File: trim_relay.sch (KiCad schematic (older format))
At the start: 27 parts, among them J1 Conn_01x01, J10 Conn_01x01, J11 Conn_01x01, J12 Conn_01x01, J2 Conn_01x01, J3 Conn_01x01, J4 Conn_01x01, J5 Conn_01x01, J6 Conn_01x01, J7 Conn_01x01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

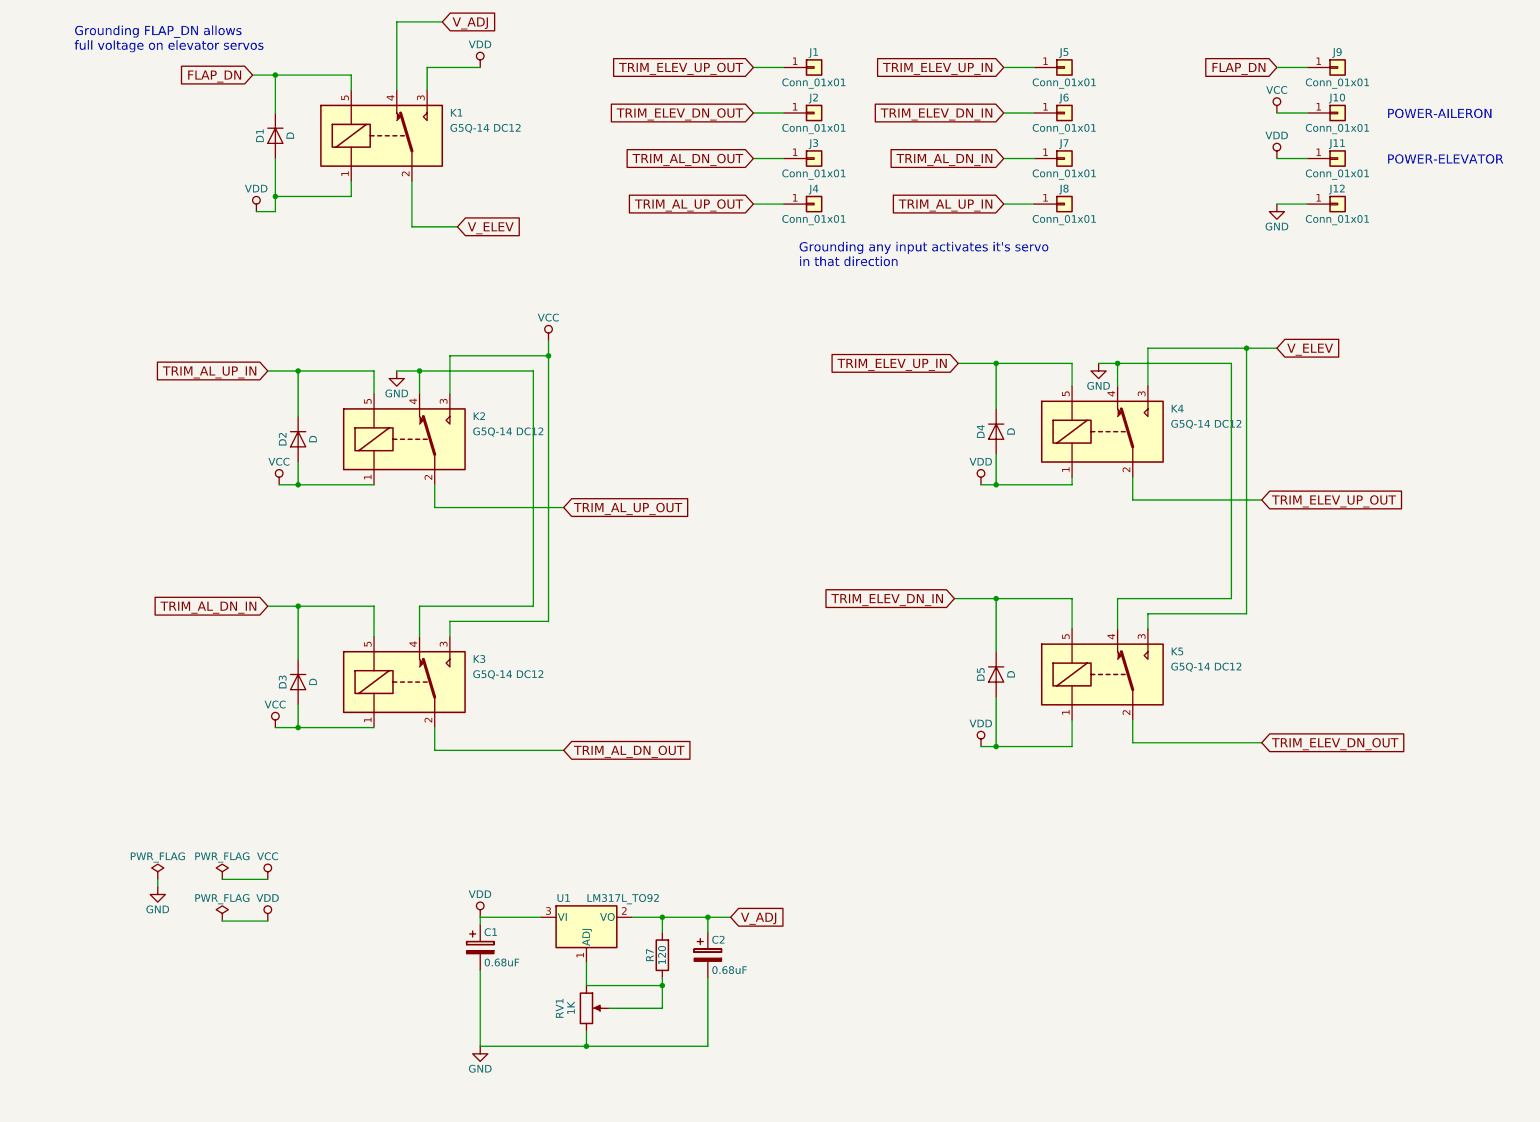
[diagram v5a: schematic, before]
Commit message: Added solder bridges, redid routing
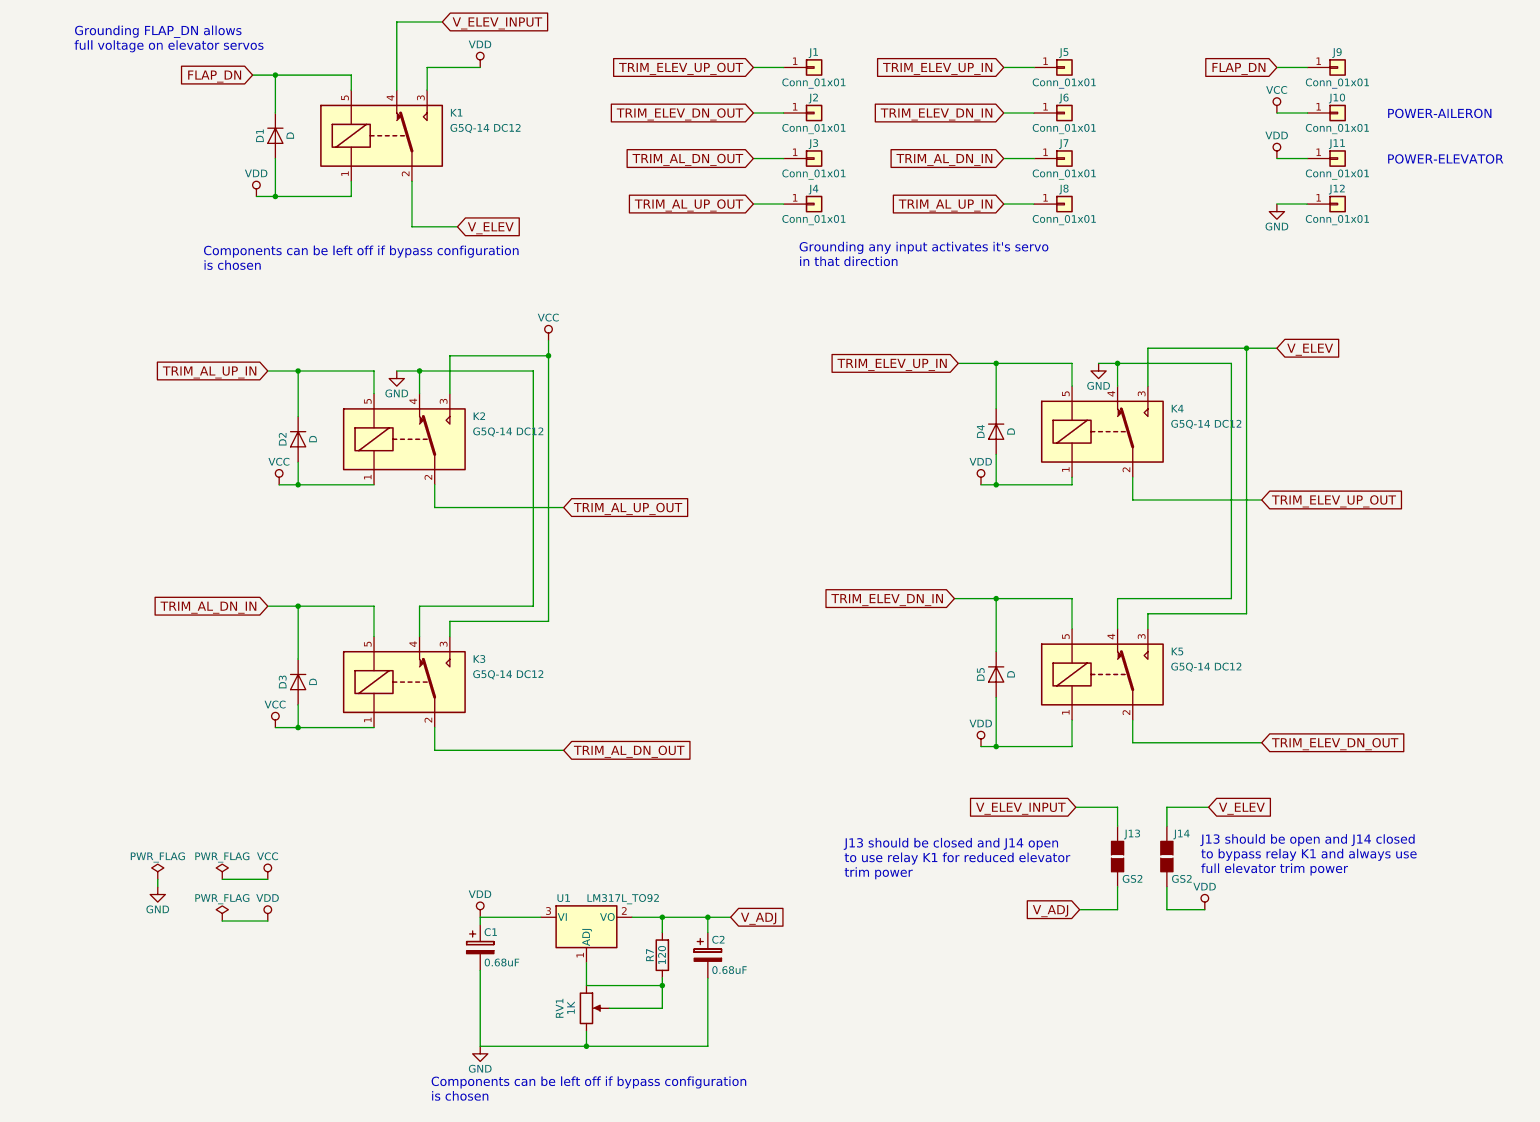
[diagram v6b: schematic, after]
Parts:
- added J13, J14: GS2, Connectors:GS2, symbol GS2
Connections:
- net VDD: now also J14.2 (G2)
- net V_ADJ: now also J13.2 (G2); no longer K1.4
- net V_ELEV: now also J14.1 (G1)
- new net V_ELEV_INPUT: J13.1 (G1), K1.4
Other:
- note added: "Components can be left off if bypass configuration\nis chosen"
- note added: "J13 should be closed and J14 open \nto use relay K1 for reduced elevator \ntrim power"
- note added: "J13 should be open and J14 closed \nto bypass relay K1 and always use \nfull elevator trim power"
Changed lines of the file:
@@
 $EndComp
-Wire Wire Line
-	2050 1550 2050 1900
 Wire Wire Line
 	2050 1250 2050 1000
@@
 TRIM_ELEV_DN_IN
 Wire Wire Line
-	8350 4450 8350 2900
+	8350 2900 8350 4450
 Wire Wire Line
 	7600 4450 7600 4650
@@
 	7700 5400 7700 5250
 $Comp
-L GND #PWR01
+L GND #PWR14
 U 1 1 5B5AE318
 P 7475 2900
-F 0 "#PWR01" H 7475 2650 50  0001 C CNN
+F 0 "#PWR14" H 7475 2650 50  0001 C CNN
 F 1 "GND" H 7475 2750 50  0000 C CNN
 F 2 "" H 7475 2900 50  0001 C CNN
@@
 Connection ~ 4100 7400
 $Comp
-L GND #PWR02
+L GND #PWR10
 U 1 1 5B5AF061
 P 3400 7400
-F 0 "#PWR02" H 3400 7150 50  0001 C CNN
+F 0 "#PWR10" H 3400 7150 50  0001 C CNN
 F 1 "GND" H 3400 7250 50  0000 C CNN
 F 2 "" H 3400 7400 50  0001 C CNN
@@
 	5200 1850 5400 1850
 Text GLabel 3150 650  2    60   Input ~ 0
-V_ADJ
+V_ELEV_INPUT
 Wire Wire Line
 	2850 650  3150 650
@@
 	8650 1850 8850 1850
 $Comp
-L GND #PWR03
+L GND #PWR18
 U 1 1 5B5FD5D6
 P 8650 1850
-F 0 "#PWR03" H 8650 1600 50  0001 C CNN
+F 0 "#PWR18" H 8650 1600 50  0001 C CNN
 F 1 "GND" H 8650 1700 50  0000 C CNN
 F 2 "" H 8650 1850 50  0001 C CNN
@@
 $EndComp
 Wire Wire Line
-	2050 1800 2550 1800
+	1925 1800 2550 1800
 Connection ~ 2050 1800
 Wire Wire Line
@@
 $EndComp
 $Comp
-L VCC #PWR04
+L VCC #PWR16
 U 1 1 5B65F2C6
 P 8650 1250
-F 0 "#PWR04" H 8650 1100 50  0001 C CNN
+F 0 "#PWR16" H 8650 1100 50  0001 C CNN
 F 1 "VCC" H 8650 1400 50  0000 C CNN
 F 2 "" H 8650 1250 50  0001 C CNN
@@
 $EndComp
 $Comp
-L VDD #PWR05
+L VDD #PWR17
 U 1 1 5B65F32E
 P 8650 1550
-F 0 "#PWR05" H 8650 1400 50  0001 C CNN
+F 0 "#PWR17" H 8650 1400 50  0001 C CNN
 F 1 "VDD" H 8650 1700 50  0000 C CNN
 F 2 "" H 8650 1550 50  0001 C CNN
@@
 POWER-AILERON
 $Comp
-L VDD #PWR06
+L VDD #PWR13
 U 1 1 5B6627AC
 P 6700 5425
-F 0 "#PWR06" H 6700 5275 50  0001 C CNN
+F 0 "#PWR13" H 6700 5275 50  0001 C CNN
 F 1 "VDD" H 6700 5575 50  0000 C CNN
 F 2 "" H 6700 5425 50  0001 C CNN
@@
 $EndComp
 $Comp
-L VDD #PWR07
+L VDD #PWR9
 U 1 1 5B6633BC
 P 3400 6550
-F 0 "#PWR07" H 3400 6400 50  0001 C CNN
+F 0 "#PWR9" H 3400 6400 50  0001 C CNN
 F 1 "VDD" H 3400 6700 50  0000 C CNN
 F 2 "" H 3400 6550 50  0001 C CNN
@@
 $EndComp
 $Comp
-L VCC #PWR08
+L VCC #PWR11
 U 1 1 5B663EC5
 P 3850 2750
-F 0 "#PWR08" H 3850 2600 50  0001 C CNN
+F 0 "#PWR11" H 3850 2600 50  0001 C CNN
 F 1 "VCC" H 3850 2900 50  0000 C CNN
 F 2 "" H 3850 2750 50  0001 C CNN
@@
 $EndComp
 $Comp
-L VCC #PWR09
+L VCC #PWR6
 U 1 1 5B664FE0
 P 2075 3700
-F 0 "#PWR09" H 2075 3550 50  0001 C CNN
+F 0 "#PWR6" H 2075 3550 50  0001 C CNN
 F 1 "VCC" H 2075 3850 50  0000 C CNN
 F 2 "" H 2075 3700 50  0001 C CNN
@@
 $EndComp
 $Comp
-L VDD #PWR010
+L VDD #PWR8
 U 1 1 5B665897
 P 3400 950
-F 0 "#PWR010" H 3400 800 50  0001 C CNN
+F 0 "#PWR8" H 3400 800 50  0001 C CNN
 F 1 "VDD" H 3400 1100 50  0000 C CNN
 F 2 "" H 3400 950 50  0001 C CNN
@@
 $EndComp
 $Comp
-L VDD #PWR011
+L VDD #PWR2
 U 1 1 5B66599E
-P 1925 1900
-F 0 "#PWR011" H 1925 1750 50  0001 C CNN
-F 1 "VDD" H 1925 2050 50  0000 C CNN
-F 2 "" H 1925 1900 50  0001 C CNN
-F 3 "" H 1925 1900 50  0001 C CNN
-	1    1925 1900
-	1    0    0    -1
-$EndComp
-Wire Wire Line
-	2050 1900 1925 1900
+P 1925 1800
+F 0 "#PWR2" H 1925 1650 50  0001 C CNN
+F 1 "VDD" H 1925 1950 50  0000 C CNN
+F 2 "" H 1925 1800 50  0001 C CNN
+F 3 "" H 1925 1800 50  0001 C CNN
+	1    1925 1800
+	1    0    0    -1
+$EndComp
 Wire Wire Line
 	2200 3250 2200 2950
@@
 	2000 4500 2700 4500
 $Comp
-L GND #PWR012
+L GND #PWR7
 U 1 1 5B6D2F47
 P 2850 2950
-F 0 "#PWR012" H 2850 2700 50  0001 C CNN
+F 0 "#PWR7" H 2850 2700 50  0001 C CNN
 F 1 "GND" H 2850 2800 50  0000 C CNN
 F 2 "" H 2850 2950 50  0001 C CNN
@@
 	3750 4500 3000 4500
 $Comp
-L VCC #PWR013
+L VCC #PWR5
 U 1 1 5B6D432D
 P 2050 5300
-F 0 "#PWR013" H 2050 5150 50  0001 C CNN
+F 0 "#PWR5" H 2050 5150 50  0001 C CNN
 F 1 "VCC" H 2050 5450 50  0000 C CNN
 F 2 "" H 2050 5300 50  0001 C CNN
@@
 $EndComp
 Wire Wire Line
-	8350 2900 7475 2900
-Wire Wire Line
-	7300 2900 6550 2900
-Wire Wire Line
-	7300 4450 6525 4450
+	7475 2900 8350 2900
+Wire Wire Line
+	6550 2900 7300 2900
+Wire Wire Line
+	6525 4450 7300 4450
 Wire Wire Line
 	6800 5425 6800 5100
 Wire Wire Line
-	7600 4450 8350 4450
+	8350 4450 7600 4450
 Wire Wire Line
 	6700 5425 7300 5425
 $Comp
-L VDD #PWR014
+L VDD #PWR12
 U 1 1 5B6D6DBC
 P 6700 3700
-F 0 "#PWR014" H 6700 3550 50  0001 C CNN
+F 0 "#PWR12" H 6700 3550 50  0001 C CNN
 F 1 "VDD" H 6700 3850 50  0000 C CNN
 F 2 "" H 6700 3700 50  0001 C CNN
@@
 	6800 3700 6800 3500
 $Comp
-L PWR_FLAG #FLG015
+L PWR_FLAG #FLG1
 U 1 1 5B6DC21E
 P 1275 6300
-F 0 "#FLG015" H 1275 6375 50  0001 C CNN
+F 0 "#FLG1" H 1275 6375 50  0001 C CNN
 F 1 "PWR_FLAG" H 1275 6450 50  0000 C CNN
 F 2 "" H 1275 6300 50  0001 C CNN
@@
 $EndComp
 $Comp
-L GND #PWR016
+L GND #PWR1
 U 1 1 5B6DC2D2
 P 1275 6350
-F 0 "#PWR016" H 1275 6100 50  0001 C CNN
+F 0 "#PWR1" H 1275 6100 50  0001 C CNN
 F 1 "GND" H 1275 6200 50  0000 C CNN
 F 2 "" H 1275 6350 50  0001 C CNN
@@
 	1275 6300 1275 6350
 $Comp
-L PWR_FLAG #FLG017
+L PWR_FLAG #FLG2
 U 1 1 5B6DC406
 P 1700 6300
-F 0 "#FLG017" H 1700 6375 50  0001 C CNN
+F 0 "#FLG2" H 1700 6375 50  0001 C CNN
 F 1 "PWR_FLAG" H 1700 6450 50  0000 C CNN
 F 2 "" H 1700 6300 50  0001 C CNN
@@
 $EndComp
 $Comp
-L VCC #PWR018
+L VCC #PWR3
 U 1 1 5B6DC78C
 P 2000 6300
-F 0 "#PWR018" H 2000 6150 50  0001 C CNN
+F 0 "#PWR3" H 2000 6150 50  0001 C CNN
 F 1 "VCC" H 2000 6450 50  0000 C CNN
 F 2 "" H 2000 6300 50  0001 C CNN
@@
 $EndComp
 $Comp
-L VDD #PWR019
+L VDD #PWR4
 U 1 1 5B6DC7E8
 P 2000 6575
-F 0 "#PWR019" H 2000 6425 50  0001 C CNN
+F 0 "#PWR4" H 2000 6425 50  0001 C CNN
 F 1 "VDD" H 2000 6725 50  0000 C CNN
 F 2 "" H 2000 6575 50  0001 C CNN
@@
 	1700 6300 2000 6300
 $Comp
-L PWR_FLAG #FLG020
+L PWR_FLAG #FLG3
 U 1 1 5B6DCB1E
 P 1700 6575
-F 0 "#FLG020" H 1700 6650 50  0001 C CNN
+F 0 "#FLG3" H 1700 6650 50  0001 C CNN
 F 1 "PWR_FLAG" H 1700 6725 50  0000 C CNN
 F 2 "" H 1700 6575 50  0001 C CNN
@@
 Wire Wire Line
 	1700 6575 2000 6575
+Wire Wire Line
+	2050 1550 2050 1800
+Text GLabel 7350 6500 0    60   Input ~ 0
+V_ADJ
+$Comp
+L VDD #PWR15
+U 1 1 5B6F2A6F
+P 8175 6500
+F 0 "#PWR15" H 8175 6350 50  0001 C CNN
+F 1 "VDD" H 8175 6650 50  0000 C CNN
+F 2 "" H 8175 6500 50  0001 C CNN
+F 3 "" H 8175 6500 50  0001 C CNN
+	1    8175 6500
+	1    0    0    -1
+$EndComp
+Text GLabel 7325 5825 0    60   Input ~ 0
+V_ELEV_INPUT
+$Comp
+L GS2 J13
+U 1 1 5B756803
+P 7600 6150
+F 0 "J13" H 7700 6300 50  0000 C CNN
+F 1 "GS2" H 7700 6001 50  0000 C CNN
+F 2 "Connectors:GS2" V 7674 6150 50  0001 C CNN
+F 3 "" H 7600 6150 50  0001 C CNN
+	1    7600 6150
+	1    0    0    -1
+$EndComp
+$Comp
+L GS2 J14
+U 1 1 5B756A07
+P 7925 6150
+F 0 "J14" H 8025 6300 50  0000 C CNN
+F 1 "GS2" H 8025 6001 50  0000 C CNN
+F 2 "Connectors:GS2" V 7999 6150 50  0001 C CNN
+F 3 "" H 7925 6150 50  0001 C CNN
+	1    7925 6150
+	1    0    0    -1
+$EndComp
+Wire Wire Line
+	7600 5950 7600 5825
+Wire Wire Line
+	7925 5825 7925 5950
+Wire Wire Line
+	7600 6350 7600 6500
+Wire Wire Line
+	7925 6350 7925 6500
+Wire Wire Line
+	7925 6500 8175 6500
+Wire Wire Line
+	7600 6500 7350 6500
+Text GLabel 8200 5825 2    60   Input ~ 0
+V_ELEV
+Wire Wire Line
+	7925 5825 8200 5825
+Wire Wire Line
+	7600 5825 7325 5825
+Text Notes 5800 6300 0    60   ~ 0
+J13 should be closed and J14 open \nto use relay K1 for reduced elevator \ntrim power
+Text Notes 8150 6275 0    60   ~ 0
+J13 should be open and J14 closed \nto bypass relay K1 and always use \nfull elevator trim power
+Text Notes 3075 7775 0    60   ~ 0
+Components can be left off if bypass configuration\nis chosen
+Text Notes 1575 2300 0    60   ~ 0
+Components can be left off if bypass configuration\nis chosen
 $EndSCHEMATC

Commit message: Final version
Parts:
- U1: footprint TO_SOT_Packages_THT:TO-92_Horizontal2_Inline_Narrow_Oval -> TO_SOT_Packages_THT:TO-220-3_Horizontal
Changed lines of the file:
@@
 	7700 5400 7700 5250
 $Comp
-L GND #PWR14
+L GND #PWR01
 U 1 1 5B5AE318
 P 7475 2900
-F 0 "#PWR14" H 7475 2650 50  0001 C CNN
+F 0 "#PWR01" H 7475 2650 50  0001 C CNN
 F 1 "GND" H 7475 2750 50  0000 C CNN
 F 2 "" H 7475 2900 50  0001 C CNN
@@
 F 0 "U1" H 3950 6675 50  0000 C CNN
 F 1 "LM317L_TO92" H 4100 6675 50  0000 L CNN
-F 2 "TO_SOT_Packages_THT:TO-92_Horizontal2_Inline_Narrow_Oval" H 4100 6775 50  0001 C CIN
+F 2 "TO_SOT_Packages_THT:TO-220-3_Horizontal" H 4100 6775 50  0001 C CIN
 F 3 "" H 4100 6550 50  0001 C CNN
 	1    4100 6550
@@
 Connection ~ 4100 7400
 $Comp
-L GND #PWR10
+L GND #PWR02
 U 1 1 5B5AF061
 P 3400 7400
-F 0 "#PWR10" H 3400 7150 50  0001 C CNN
+F 0 "#PWR02" H 3400 7150 50  0001 C CNN
 F 1 "GND" H 3400 7250 50  0000 C CNN
 F 2 "" H 3400 7400 50  0001 C CNN
@@
 	8650 1850 8850 1850
 $Comp
-L GND #PWR18
+L GND #PWR03
 U 1 1 5B5FD5D6
 P 8650 1850
-F 0 "#PWR18" H 8650 1600 50  0001 C CNN
+F 0 "#PWR03" H 8650 1600 50  0001 C CNN
 F 1 "GND" H 8650 1700 50  0000 C CNN
 F 2 "" H 8650 1850 50  0001 C CNN
@@
 $EndComp
 $Comp
-L VCC #PWR16
+L VCC #PWR04
 U 1 1 5B65F2C6
 P 8650 1250
-F 0 "#PWR16" H 8650 1100 50  0001 C CNN
+F 0 "#PWR04" H 8650 1100 50  0001 C CNN
 F 1 "VCC" H 8650 1400 50  0000 C CNN
 F 2 "" H 8650 1250 50  0001 C CNN
@@
 $EndComp
 $Comp
-L VDD #PWR17
+L VDD #PWR05
 U 1 1 5B65F32E
 P 8650 1550
-F 0 "#PWR17" H 8650 1400 50  0001 C CNN
+F 0 "#PWR05" H 8650 1400 50  0001 C CNN
 F 1 "VDD" H 8650 1700 50  0000 C CNN
 F 2 "" H 8650 1550 50  0001 C CNN
@@
 POWER-AILERON
 $Comp
-L VDD #PWR13
+L VDD #PWR06
 U 1 1 5B6627AC
 P 6700 5425
-F 0 "#PWR13" H 6700 5275 50  0001 C CNN
+F 0 "#PWR06" H 6700 5275 50  0001 C CNN
 F 1 "VDD" H 6700 5575 50  0000 C CNN
 F 2 "" H 6700 5425 50  0001 C CNN
@@
 $EndComp
 $Comp
-L VDD #PWR9
+L VDD #PWR07
 U 1 1 5B6633BC
 P 3400 6550
-F 0 "#PWR9" H 3400 6400 50  0001 C CNN
+F 0 "#PWR07" H 3400 6400 50  0001 C CNN
 F 1 "VDD" H 3400 6700 50  0000 C CNN
 F 2 "" H 3400 6550 50  0001 C CNN
@@
 $EndComp
 $Comp
-L VCC #PWR11
+L VCC #PWR08
 U 1 1 5B663EC5
 P 3850 2750
-F 0 "#PWR11" H 3850 2600 50  0001 C CNN
+F 0 "#PWR08" H 3850 2600 50  0001 C CNN
 F 1 "VCC" H 3850 2900 50  0000 C CNN
 F 2 "" H 3850 2750 50  0001 C CNN
@@
 $EndComp
 $Comp
-L VCC #PWR6
+L VCC #PWR09
 U 1 1 5B664FE0
 P 2075 3700
-F 0 "#PWR6" H 2075 3550 50  0001 C CNN
+F 0 "#PWR09" H 2075 3550 50  0001 C CNN
 F 1 "VCC" H 2075 3850 50  0000 C CNN
 F 2 "" H 2075 3700 50  0001 C CNN
@@
 $EndComp
 $Comp
-L VDD #PWR8
+L VDD #PWR010
 U 1 1 5B665897
 P 3400 950
-F 0 "#PWR8" H 3400 800 50  0001 C CNN
+F 0 "#PWR010" H 3400 800 50  0001 C CNN
 F 1 "VDD" H 3400 1100 50  0000 C CNN
 F 2 "" H 3400 950 50  0001 C CNN
@@
 $EndComp
 $Comp
-L VDD #PWR2
+L VDD #PWR011
 U 1 1 5B66599E
 P 1925 1800
-F 0 "#PWR2" H 1925 1650 50  0001 C CNN
+F 0 "#PWR011" H 1925 1650 50  0001 C CNN
 F 1 "VDD" H 1925 1950 50  0000 C CNN
 F 2 "" H 1925 1800 50  0001 C CNN
@@
 	2000 4500 2700 4500
 $Comp
-L GND #PWR7
+L GND #PWR012
 U 1 1 5B6D2F47
 P 2850 2950
-F 0 "#PWR7" H 2850 2700 50  0001 C CNN
+F 0 "#PWR012" H 2850 2700 50  0001 C CNN
 F 1 "GND" H 2850 2800 50  0000 C CNN
 F 2 "" H 2850 2950 50  0001 C CNN
@@
 	3750 4500 3000 4500
 $Comp
-L VCC #PWR5
+L VCC #PWR013
 U 1 1 5B6D432D
 P 2050 5300
-F 0 "#PWR5" H 2050 5150 50  0001 C CNN
+F 0 "#PWR013" H 2050 5150 50  0001 C CNN
 F 1 "VCC" H 2050 5450 50  0000 C CNN
 F 2 "" H 2050 5300 50  0001 C CNN
@@
 	6700 5425 7300 5425
 $Comp
-L VDD #PWR12
+L VDD #PWR014
 U 1 1 5B6D6DBC
 P 6700 3700
-F 0 "#PWR12" H 6700 3550 50  0001 C CNN
+F 0 "#PWR014" H 6700 3550 50  0001 C CNN
 F 1 "VDD" H 6700 3850 50  0000 C CNN
 F 2 "" H 6700 3700 50  0001 C CNN
@@
 	6800 3700 6800 3500
 $Comp
-L PWR_FLAG #FLG1
+L PWR_FLAG #FLG015
 U 1 1 5B6DC21E
 P 1275 6300
-F 0 "#FLG1" H 1275 6375 50  0001 C CNN
+F 0 "#FLG015" H 1275 6375 50  0001 C CNN
 F 1 "PWR_FLAG" H 1275 6450 50  0000 C CNN
 F 2 "" H 1275 6300 50  0001 C CNN
@@
 $EndComp
 $Comp
-L GND #PWR1
+L GND #PWR016
 U 1 1 5B6DC2D2
 P 1275 6350
-F 0 "#PWR1" H 1275 6100 50  0001 C CNN
+F 0 "#PWR016" H 1275 6100 50  0001 C CNN
 F 1 "GND" H 1275 6200 50  0000 C CNN
 F 2 "" H 1275 6350 50  0001 C CNN
@@
 	1275 6300 1275 6350
 $Comp
-L PWR_FLAG #FLG2
+L PWR_FLAG #FLG017
 U 1 1 5B6DC406
 P 1700 6300
-F 0 "#FLG2" H 1700 6375 50  0001 C CNN
+F 0 "#FLG017" H 1700 6375 50  0001 C CNN
 F 1 "PWR_FLAG" H 1700 6450 50  0000 C CNN
 F 2 "" H 1700 6300 50  0001 C CNN
@@
 $EndComp
 $Comp
-L VCC #PWR3
+L VCC #PWR018
 U 1 1 5B6DC78C
 P 2000 6300
-F 0 "#PWR3" H 2000 6150 50  0001 C CNN
+F 0 "#PWR018" H 2000 6150 50  0001 C CNN
 F 1 "VCC" H 2000 6450 50  0000 C CNN
 F 2 "" H 2000 6300 50  0001 C CNN
@@
 $EndComp
 $Comp
-L VDD #PWR4
+L VDD #PWR019
 U 1 1 5B6DC7E8
 P 2000 6575
-F 0 "#PWR4" H 2000 6425 50  0001 C CNN
+F 0 "#PWR019" H 2000 6425 50  0001 C CNN
 F 1 "VDD" H 2000 6725 50  0000 C CNN
 F 2 "" H 2000 6575 50  0001 C CNN
@@
 	1700 6300 2000 6300
 $Comp
-L PWR_FLAG #FLG3
+L PWR_FLAG #FLG020
 U 1 1 5B6DCB1E
 P 1700 6575
-F 0 "#FLG3" H 1700 6650 50  0001 C CNN
+F 0 "#FLG020" H 1700 6650 50  0001 C CNN
 F 1 "PWR_FLAG" H 1700 6725 50  0000 C CNN
 F 2 "" H 1700 6575 50  0001 C CNN
@@
 V_ADJ
 $Comp
-L VDD #PWR15
+L VDD #PWR021
 U 1 1 5B6F2A6F
 P 8175 6500
-F 0 "#PWR15" H 8175 6350 50  0001 C CNN
+F 0 "#PWR021" H 8175 6350 50  0001 C CNN
 F 1 "VDD" H 8175 6650 50  0000 C CNN
 F 2 "" H 8175 6500 50  0001 C CNN
